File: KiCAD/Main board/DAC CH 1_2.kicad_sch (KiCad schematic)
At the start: 48 parts, among them IC1 OPA1632DR, IC2 PCM1789-Q1, U1 LM4562

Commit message: KICAD
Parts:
- removed C1, C10, C11, C9: C, symbol Device:C
- added C1, C15, C16, C20, C22, C33, C34, C4, C5: 22uF, Capacitor_THT:CP_Radial_D5.0mm_P2.00mm, symbol Device:C_Polarized
- added C14, C29: 2.2n, Capacitor_SMD:C_0805_2012Metric, symbol Device:C
- added C17: 1N, Capacitor_SMD:C_0805_2012Metric, symbol Device:C
- added C18: 680p, Capacitor_SMD:C_0805_2012Metric, symbol Device:C
- added C19, C21, C23, C24, C31, C32, C6: 100nF, Capacitor_SMD:C_0805_2012Metric, symbol Device:C
- added C27: 680, Capacitor_SMD:C_0805_2012Metric, symbol Device:C
- added R31, R32, R33, R34, R35, R39, R40: 10, Resistor_SMD:R_0805_2012Metric, symbol Device:R
- added R37: 39, Resistor_SMD:R_0805_2012Metric, symbol Device:R
- C10: renamed from C7; value C -> 680p; footprint (none) -> Capacitor_SMD:C_0805_2012Metric
- C11: renamed from C8; value C -> 680; footprint (none) -> Capacitor_SMD:C_0805_2012Metric
- C12: value C -> 2.2n; footprint (none) -> Capacitor_SMD:C_0805_2012Metric
- C13: value C -> 5.6n; footprint (none) -> Capacitor_SMD:C_0805_2012Metric
- C2, C3: value C -> 100nF; footprint (none) -> Capacitor_SMD:C_0805_2012Metric
- C7: renamed from C4; value C -> 5.6n; footprint (none) -> Capacitor_SMD:C_0805_2012Metric
- C8: renamed from C5; value C -> 2.2n; footprint (none) -> Capacitor_SMD:C_0805_2012Metric
- C9: renamed from C6; value C -> 1N; footprint (none) -> Capacitor_SMD:C_0805_2012Metric
- R10, R29: value R -> 22
- R11, R28: value R -> 4.3K
- R12, R16, R20, R21: value R -> 1k
- R13, R17, R22, R27: value R -> 4.7k
- R14, R15, R30: value R -> 39
- R18, R19, R5, R6: value R -> 10K
- R23, R9: value R -> 4.3k
- R24: value R -> 10
- R25, R26, R7, R8: value R -> 820
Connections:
- net ADR0 is gone; now on net GND: IC2.23 (MS/ADR0/RSV)
- net ADR1 is gone; now on net GND: IC2.24 (ADR5/ADR1/RSV)
- net +12V: now also R24.1, R32.2, R40.1; no longer IC1.3 (V+), IC1.3 (V+), U1.8 (V+)
- net +3.3V: now also C19.1, C20.1; no longer C2.1, C2.2, C3.1, C3.2, C8.2, IC1.2 (VOCM), IC1.2 (VOCM), IC1.9 (GND), IC1.9 (GND), IC2.10 (AGND1), IC2.15 (AGND2), IC2.16 (VCC2), IC2.7 (DGND), IC2.8 (VCC1), R23.2, R9.2
- net -12V: now also R31.1, R35.1, R39.2; no longer IC1.6 (V-), IC1.6 (V-), U1.4 (V-)
- net at R25.2, U1.3 (+): now also C17.1
- net at IC1.1 (VIN-), R22.1: now also R20.2, C27.1; no longer C13.1, R18.2
- net at IC1.8 (VIN+), R21.2: now also R27.1, C18.1; no longer C12.1, R26.1
- net at R24.2: now also IC1.3 (V+), C15.2, C23.2; no longer U1.2 (-)
- net at IC2.13 (VOUTR+), R21.1: now also R19.1; no longer R20.1
- net GND: now reaches IC1.7 (ENABLE)
- net GND: now also C2.2, C3.2, C8.2, IC1.2 (VOCM), IC1.2 (VOCM), IC1.7 (ENABLE), IC1.9 (GND), IC1.9 (GND), IC2.10 (AGND1), IC2.15 (AGND2), IC2.16 (VCC2), IC2.7 (DGND), IC2.8 (VCC1), R23.2, R9.2, C1.2, C14.2, C15.1, C16.2, C19.2, C20.2, C21.1, C22.1, C23.1, C24.2, C31.2, C32.1, C33.2, C34.1, C4.2, C5.2, C6.2
- net RCA JACK L renamed RCA JACK CH1
- net RCA JACK CH1: now also R29.2
- net RCA/JACK R: no longer names the net of R28.2
- net RCA/JACK R: now also R29.1, U1.1, C17.2
- net VOUTL+ renamed VOUT CH1(+)
- net VOUT CH1(+): now also C12.2, R22.2, C29.2, R37.2
- net VOUTL- renamed VOUT CH1(-)
- net VOUT CH1(-): now also C12.1, R27.2, R30.2, C29.1
- removed net VOUTR+: R22.2, R30.2
- net VOUTR-: no longer names the net of R26.2
- net VOUTR-: now also U1.2 (-), C14.1; no longer R29.2
- new net: C13.2, R19.2, R23.1, R26.1
- new net: C1.1, C3.1, R34.1
- new net: C4.1, C6.1, R32.1, U1.8 (V+)
- new net: C31.1, C33.1, IC1.6 (V-), R39.1
- new net: C32.2, C34.2, IC1.3 (V+), R40.2
- new net: C27.2, IC1.4 (VOUT+), R37.1
- new net: C18.2, IC1.5 (VOUT-), R30.1
- new net: C16.1, C24.1, IC1.6 (V-), R35.2
- new net: IC2.14 (VOUTR-), R18.2, R20.1
- new net: C13.1, R18.1, R25.1, R28.1
- new net: C21.2, C22.2, R31.2, U1.4 (V-)
- new net: C2.1, C5.1, R33.1
- new net +5V: R33.2, R34.2
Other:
- note added: "Decoupling capacitors (100nF and 22uF)(power supply) -100nF X7R ceremic capacitor-> 0805 mabye we change it to 0402 later -22uF TH electrolytic"
- note added: "Filter capacitors for with small capacitance -Type C0G - NP0 -Footprint 0805 (mabye we change it to 0402 later)"
- moved on the sheet: C10, C11, C7, C8, C9, IC1, IC2, R1, R10, R11, R12, R13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

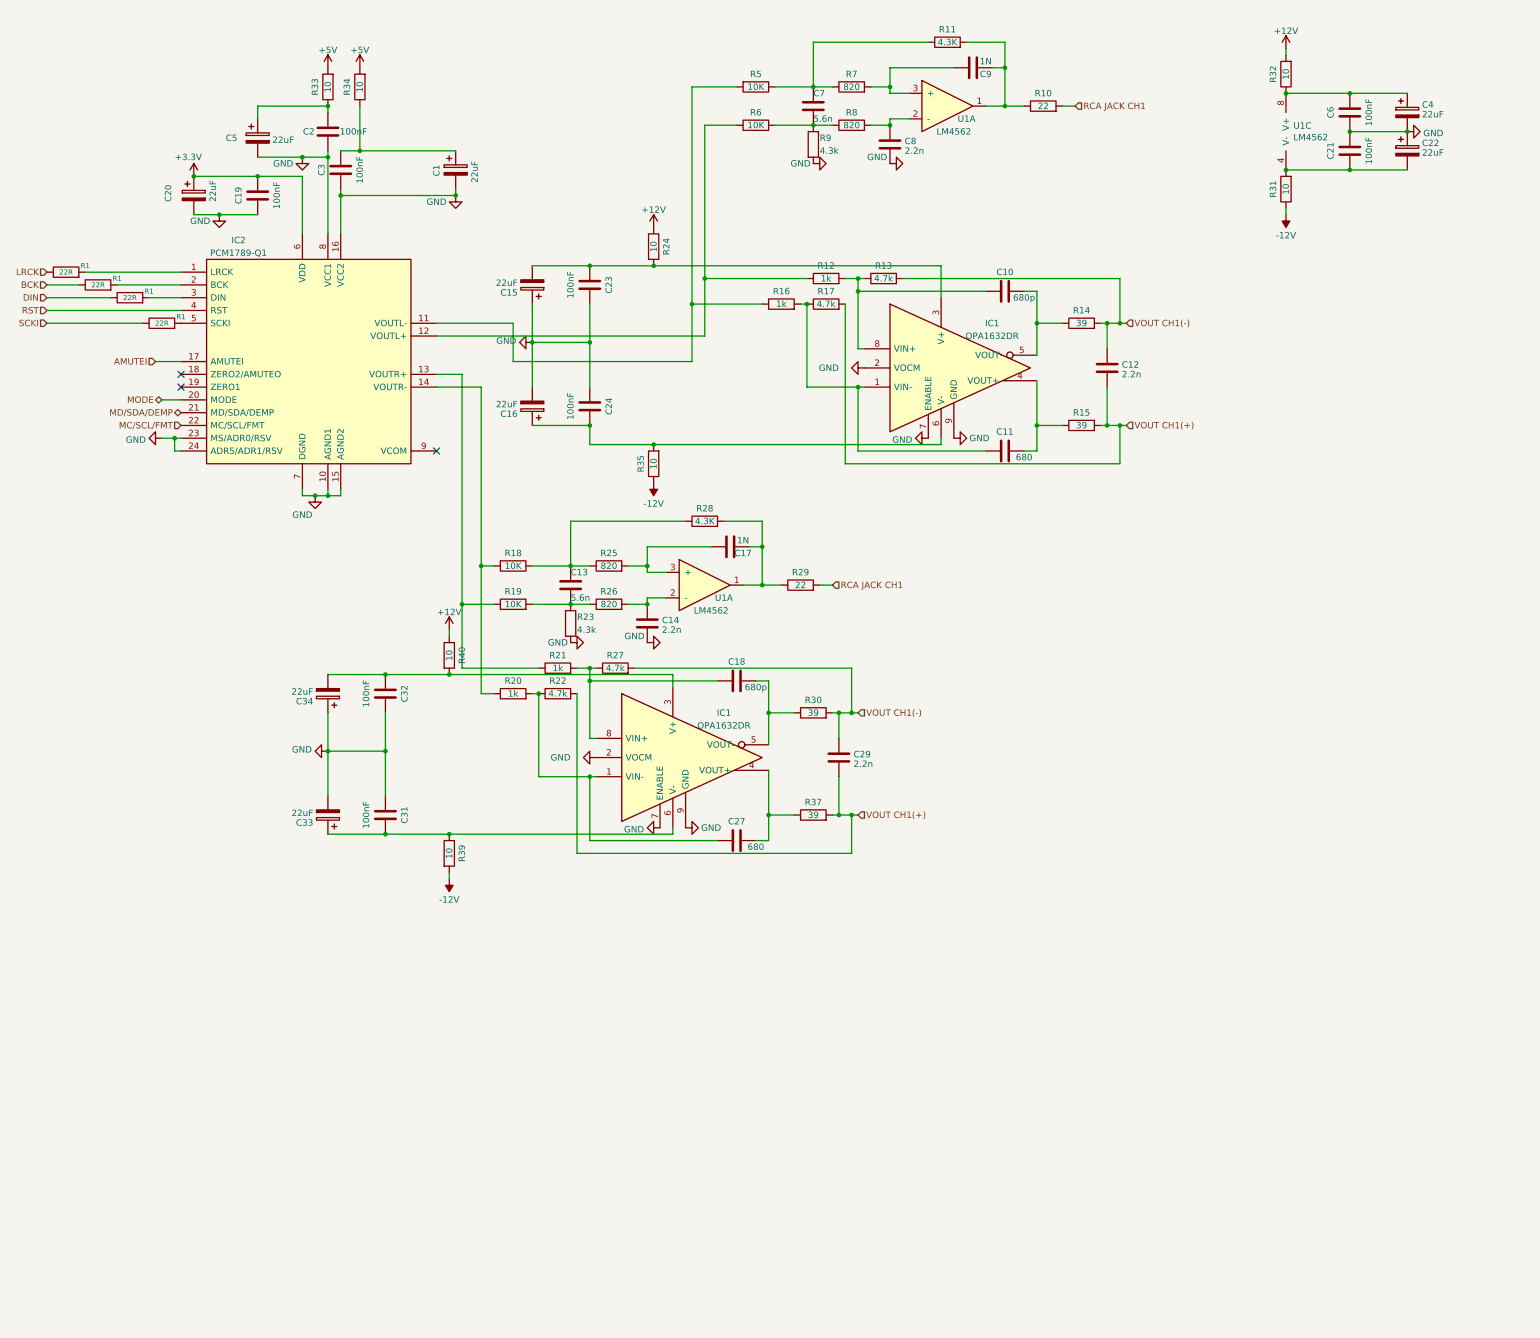
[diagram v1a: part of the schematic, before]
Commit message: Updated KiCAD library and main board schematic
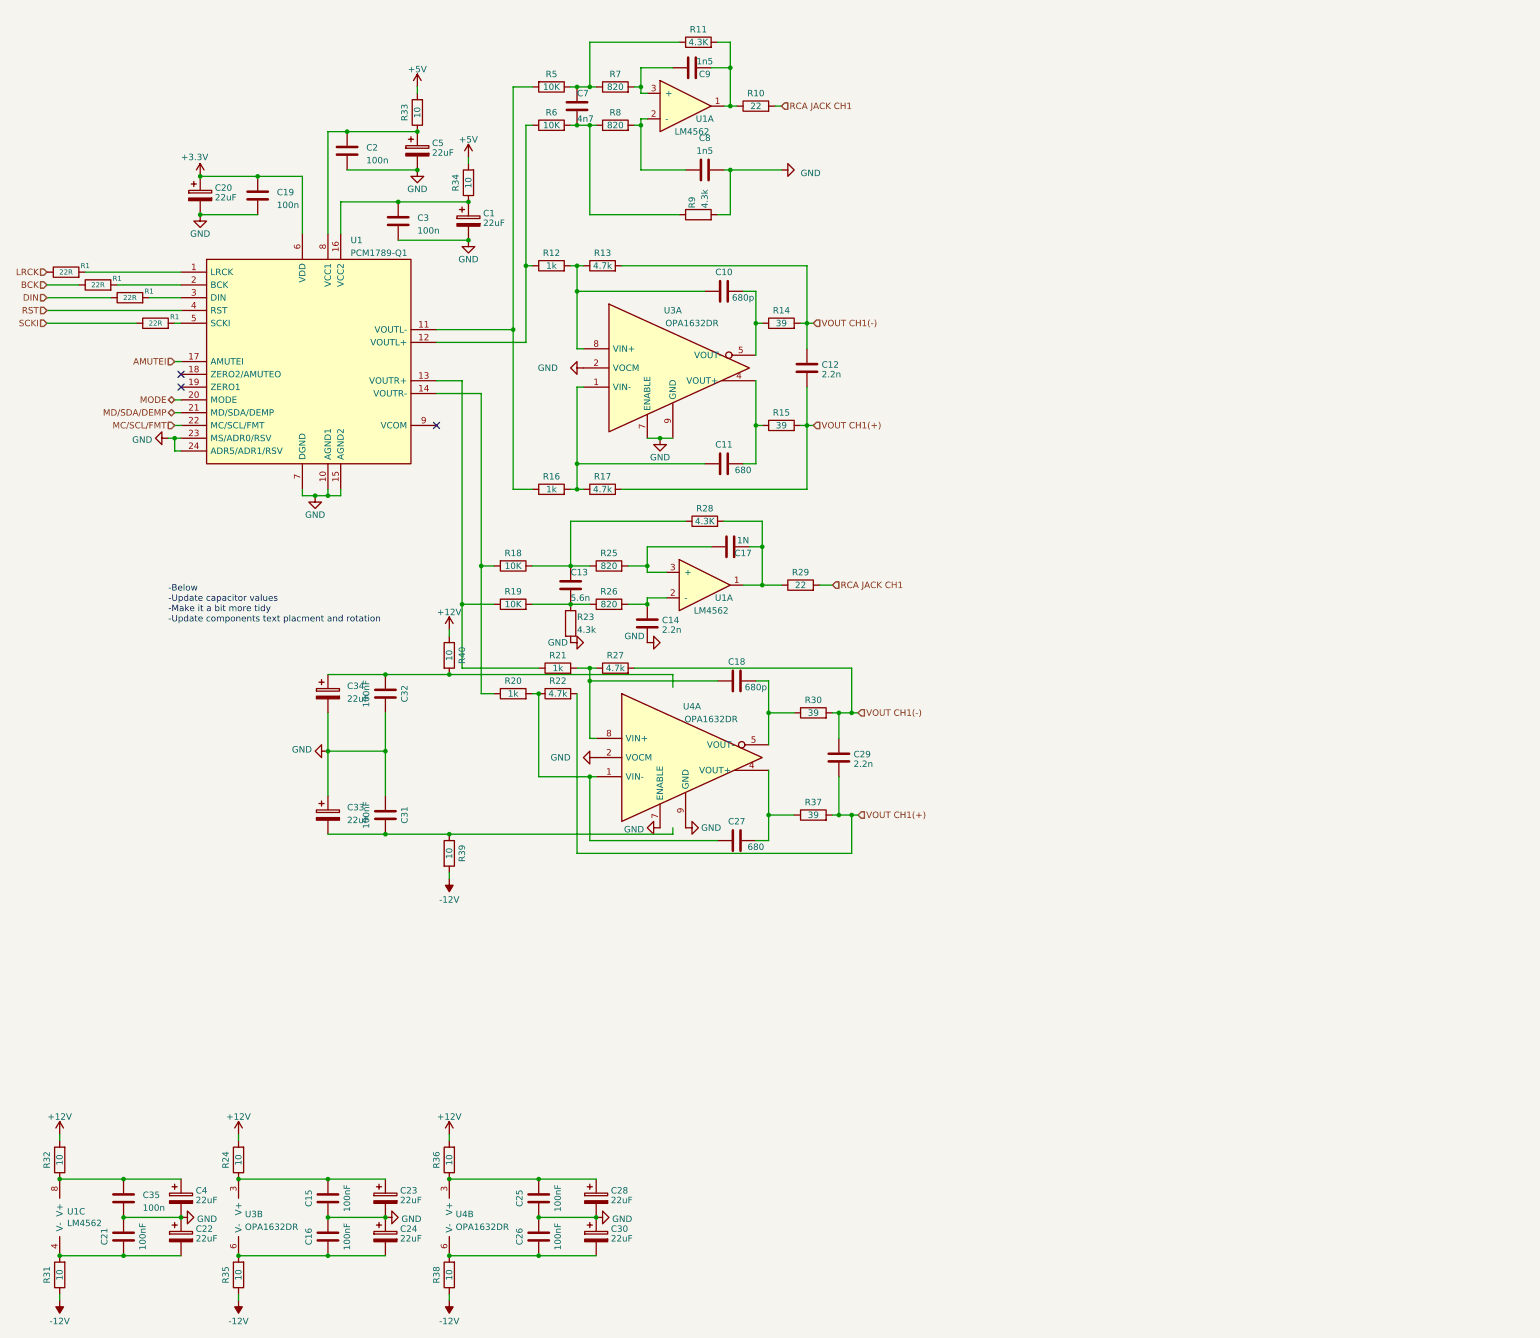
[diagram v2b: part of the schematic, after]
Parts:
- removed C15, C16: 22uF, Capacitor_THT:CP_Radial_D5.0mm_P2.00mm, symbol Device:C_Polarized
- removed C23, C24, C6: 100nF, Capacitor_SMD:C_0805_2012Metric, symbol Device:C
- removed IC1 (x2): OPA1632DR, Audio_DSP:VSSOP-8_3.0x3.0mm_P0.65_TP1.8x1.5, symbol Main board-rescue:OPA1632DR-Audio_DSP
- removed IC2: PCM1789-Q1, Package_SO:TSSOP-24_4.4x7.8mm_P0.65mm, symbol Main board-rescue:PCM1789-Q1-Audio_DSP
- added C15, C16, C25, C26: 100nF, Capacitor_SMD:C_0805_2012Metric, symbol Device:C
- added C23, C24, C28, C30: 22uF, Capacitor_THT:CP_Radial_D5.0mm_P2.00mm, symbol Device:C_Polarized
- added C35: 100n, Capacitor_SMD:C_0805_2012Metric, symbol Device:C
- added R36, R38: 10, Resistor_SMD:R_0805_2012Metric, symbol Device:R
- added U1: PCM1789-Q1, Package_SO:TSSOP-24_4.4x7.8mm_P0.65mm, symbol Audio-DSP:PCM1789-Q1
- added U3, U4: OPA1632DR, Audio_DSP:VSSOP-8_3.0x3.0mm_P0.65_TP1.8x1.5, symbol Audio-DSP:OPA1632DR
- C19, C2, C3: value 100nF -> 100n
- C7: value 5.6n -> 4n7
- C8: value 2.2n -> 1n5
- C9: value 1N -> 1n5
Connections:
- net +12V: now also R24.2, R36.2; no longer R24.1
- net +3.3V: now also U1.6 (VDD)
- net -12V: now also R38.1
- net AMUTEI: now also U1.17 (AMUTEI)
- net GND: now also C33.1, C34.2, C15.2, C16.1, C23.2, C24.1, C25.2, C26.1, C28.2, C30.1, C35.2, U1.10 (AGND1), U1.15 (AGND2), U1.23 (MS/ADR0/RSV), U1.24 (ADR5/ADR1/RSV), U1.7 (DGND), U3.2 (VOCM), U3.7 (ENABLE), U3.9 (GND), U4.2 (VOCM), U4.7 (ENABLE), U4.9 (GND); no longer C33.2, C34.1
- net MC/SCL/FMT: now also U1.22 (MC/SCL/FMT)
- net MD/SDA/DEMP: now also U1.21 (MD/SDA/DEMP)
- net MODE: now also U1.20 (MODE)
- net RST: now also U1.4 (RST)
- net at C11.1, R16.2, R17.1: now also U3.1 (VIN-)
- net at R19.1, R21.1: now also U1.13 (VOUTR+)
- net at C1.1, C3.1, R34.1: now also U1.16 (VCC2)
- net at R12.1, R6.1: now also U1.12 (VOUTL+)
- net at C4.1, R32.1, U1.8 (V+): now also C35.1
- net at C31.1, R39.1: now also C33.2; no longer C33.1
- net at C10.1, R12.2, R13.1: now also U3.8 (VIN+)
- net at C32.2, R40.2: now also C34.1; no longer C34.2
- net at C27.1, R20.2, R22.1: now also U4.1 (VIN-)
- net at C27.2, R37.1: now also U4.4 (VOUT+)
- net at C18.2, R30.1: now also U4.5 (VOUT-)
- net at C18.1, R21.2, R27.1: now also U4.8 (VIN+)
- net at R35.2: now also C16.2, C24.2, U3.6 (V-)
- net at R1.2: now also U1.2 (BCK)
- net at C10.2, R14.1: now also U3.5 (VOUT-)
- net at R18.2, R20.1: now also U1.14 (VOUTR-)
- net at R16.1, R5.2: now also U1.11 (VOUTL-)
- net at C2.1, C5.1, R33.1: now also U1.8 (VCC1)
- net at R1.2: now also U1.1 (LRCK)
- net at C11.2, R15.1: now also U3.4 (VOUT+)
- net at R1.2: now also U1.3 (DIN)
- net at R1.2: now also U1.5 (SCKI)
- new net: C25.1, C28.1, R36.1, U4.3 (V+)
- new net: C15.1, C23.1, R24.1, U3.3 (V+)
- new net: C26.2, C30.2, R38.2, U4.6 (V-)
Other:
- note added: "-Below -Update capacitor values -Make it a bit more tidy -Update components text placment and rotation"
- moved on the sheet: C10, C11, C12, C21, C22, C33, C34, C4, C7, C8, C9, R1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
